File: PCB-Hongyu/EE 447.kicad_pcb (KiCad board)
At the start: 4 copper layers, 100 x 100 mm, 73 parts, among them J1 Conn_01x04_Pin, J2 503480-2600, J3 S2B-PH-SM4-TB, J5 Conn_01x02_Pin, J6 Conn_01x01_Pin, J7 Conn_01x01_Pin, J8 Conn_01x01_Pin, J9 Conn_01x02_Pin, Q1 BSS138, Q2 S8050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

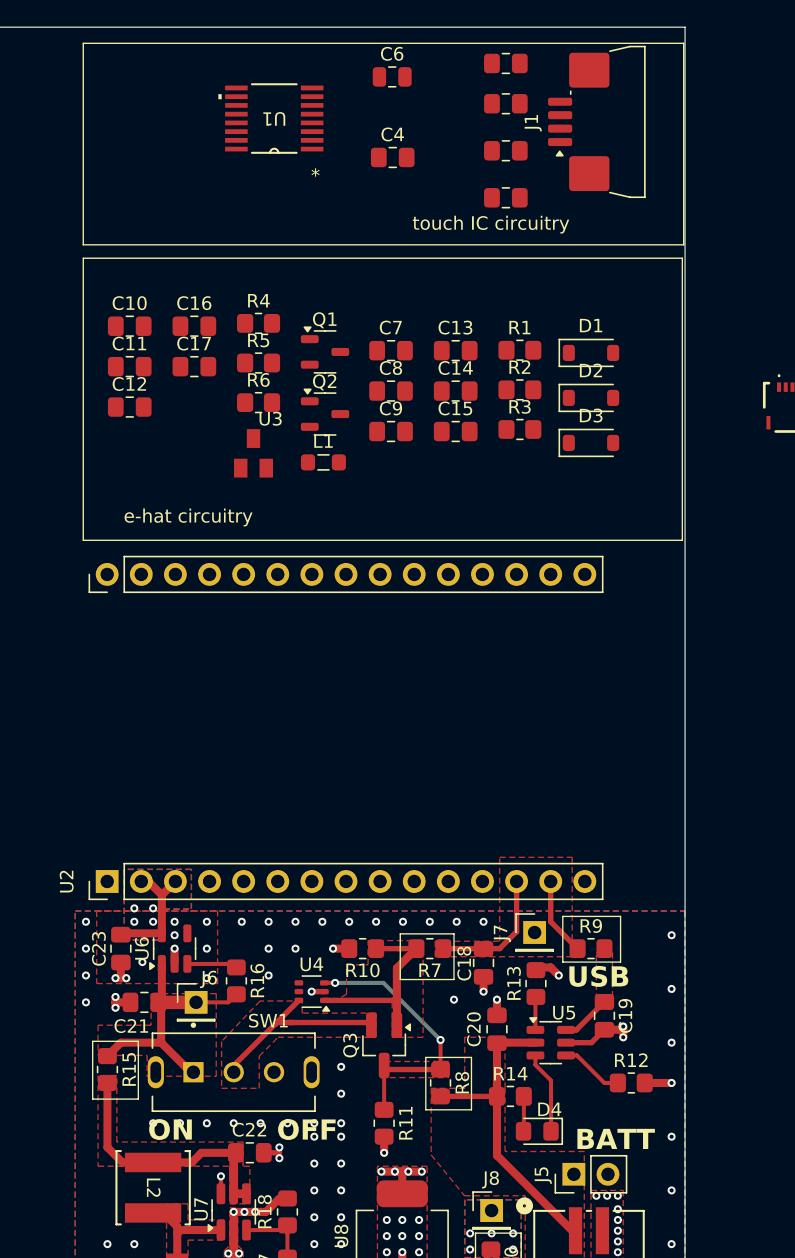
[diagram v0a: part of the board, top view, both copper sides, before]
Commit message: touch ic mostly routed
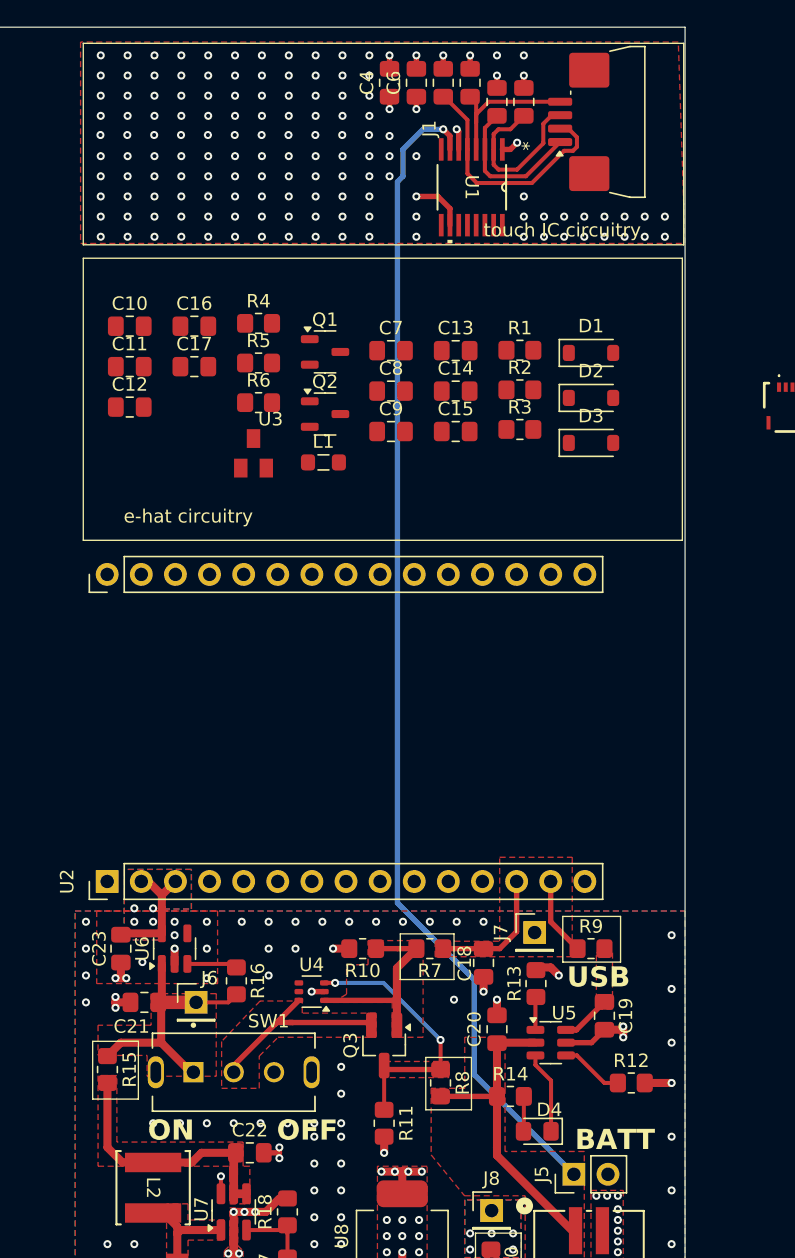
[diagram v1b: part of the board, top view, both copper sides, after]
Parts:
- C6: footprint Capacitor_SMD:C_0805_2012Metric -> Capacitor_SMD:C_0805_2012Metric_Pad1.18x1.45mm_HandSolder
- moved U1 15.6 mm to (215.1, 115.3), turned to -90 degrees
- moved C2 7.17 mm to (217.0, 109.0), turned to 90 degrees
- moved C5 6.88 mm to (213.0, 107.5), turned to 90 degrees
- moved C4 5.57 mm to (209.0, 107.5), turned to 90 degrees
- moved C3 3.03 mm to (215.0, 107.5), turned to 90 degrees
- moved C6 1.85 mm to (211.0, 107.5), turned to 90 degrees
- moved C1 1.34 mm to (219.0, 109.0), turned to 90 degrees
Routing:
- net +BATT: track 23.8 -> 111.0 mm, vias 0 -> 1
- net Net-(J1-Pin_2): track 0.00 -> 18.3 mm
- net Net-(J1-Pin_3): track 0.00 -> 12.8 mm
- net Net-(J1-Pin_4): track 0.00 -> 11.4 mm
- net Net-(J1-Pin_1): track 0.00 -> 11.3 mm
- net GND: track 48.3 -> 55.5 mm, vias 121 -> 263
- net +3.3V: track 9.32 -> 13.4 mm, vias 4 -> 5
- net +5V: track 0.00 -> 3.16 mm, vias 5 -> 8

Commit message: footprints
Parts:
- J2: value 503480-2600 -> FH34SRJ-24S-0.5SH_99_; footprint Custom:5034802600 -> Custom:FH34SRJ24S05SH99
- Q2: footprint Package_TO_SOT_SMD:SOT-23-3 -> Package_TO_SOT_THT:TO-92_Inline
- moved U3 68.8 mm to (267.6, 138.1)
- moved Q2 64.2 mm to (268.3, 129.0)
- moved Q1 59.8 mm to (263.1, 138.2)
- moved R4 59.8 mm to (258.1, 136.1)
- moved R5 59.8 mm to (258.1, 139.0)
- moved R6 59.8 mm to (258.1, 142.0)
- moved L1 59.2 mm to (263.0, 141.8)
- moved C11 59.0 mm to (248.5, 132.9)
- moved C17 59.0 mm to (253.3, 132.9)
- moved C10 59.0 mm to (248.5, 129.9)
- moved C12 59.0 mm to (248.5, 135.9)
- moved C16 59.0 mm to (253.3, 129.9)
- moved C13 40.0 mm to (253.3, 120.9)
- moved C14 40.0 mm to (253.3, 123.9)
- moved C15 40.0 mm to (253.3, 126.9)
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- renumbered J8 to J4, J9 to J8
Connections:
- net /Epaper/EPD_PWR renamed Net-(R3-Pad2)
- net CS_EPD renamed /Epaper/EPD_CS
- C10 pad 1: 3V3_EPD -> /Epaper/3V3_OUT
- C10 pad 2: GND -> /Epaper/BS
- C11 pad 2: GND -> /Epaper/BS
- C12 pad 2: GND -> /Epaper/BS
- C13 pad 2: GND -> /Epaper/BS
- C14 pad 2: GND -> /Epaper/BS
- C15 pad 2: GND -> /Epaper/BS
- C16 pad 2: GND -> /Epaper/BS
- C17 pad 1: +3.3V -> /Epaper/VCC_INT
- C17 pad 2: GND -> /Epaper/BS
- C7 pad 1: GND -> /Epaper/BS
- C7 pad 2: 3V3_EPD -> Net-(C7-Pad2)
- C9 pad 2: GND -> /Epaper/BS
- D1 pad 1: GND -> /Epaper/BS
- J2 pad 13: CLK -> /Epaper/EPD_SCK
- J2 pad 14: MOSI -> /Epaper/EPD_DIN
- J2 pad 15: 3V3_EPD -> /Epaper/3V3_OUT
- J2 pad 16: 3V3_EPD -> /Epaper/3V3_OUT
- J2 pad 17: GND -> /Epaper/BS
- J2 pad 8: GND -> /Epaper/BS
- J2 pad MP1: unconnected-(J2-MP1_1-PadMP1) -> /Epaper/BS
- J2 pad MP2: unconnected-(J2-MP1_2-PadMP2) -> /Epaper/BS
- L1 pad 1: 3V3_EPD -> Net-(C7-Pad2)
- Q1 pad 1: /Epaper/GDR -> Net-(Q1-G)
- Q1 pad 2: /Epaper/RESE -> Net-(Q1-S)
- Q2 pad 1: GND -> /Epaper/BS
- R1 pad 1: /Epaper/RESE -> Net-(Q1-S)
- R1 pad 2: GND -> /Epaper/BS
- R2 pad 1: GND -> /Epaper/BS
- R2 pad 2: /Epaper/GDR -> Net-(Q1-G)
- R3 pad 1: +3.3V -> /Epaper/VCC_INT
- R5 pad 1: +3.3V -> /Epaper/VCC_INT
- R6 pad 1: GND -> /Epaper/BS
- U3 pad 2: +3.3V -> /Epaper/VCC_INT
- U3 pad 3: 3V3_EPD -> unconnected-(U3-Pad3)

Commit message: adapter
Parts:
- added J9: 61302421121, Custom:61302421121, F.Cu at (144.5, 132.6)
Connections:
- net Net-(C11-Pad1) renamed /Epaper/SUB18
- net Net-(C12-Pad1) renamed /Epaper/SUB20
- net Net-(C14-Pad1) renamed /Epaper/SUB22
- net Net-(C16-Pad1) renamed /Epaper/SUB24
- net Net-(C9-Pad1) renamed /Epaper/SUB5

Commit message: i added stuff
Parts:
- moved J9 91.6 mm to (235.0, 118.4), turned to -90 degrees
- moved Q2 58.9 mm to (209.4, 127.3), turned to 90 degrees
- moved L1 57.1 mm to (206.0, 137.8), turned to -90 degrees
- moved U3 55.3 mm to (214.5, 123.0)
- moved D3 54.4 mm to (209.2, 130.5), turned to 180 degrees
- moved Q1 54.4 mm to (208.9, 133.8), turned to 180 degrees
- moved D1 54.2 mm to (210.5, 139.0), turned to -90 degrees
- moved D2 49.6 mm to (214.5, 138.8), turned to 90 degrees
- moved R1 45.5 mm to (213.0, 133.3)
- moved R2 45.4 mm to (213.0, 135.3), turned to 180 degrees
- moved R5 45.4 mm to (214.5, 126.5), turned to 180 degrees
- moved R6 45.0 mm to (214.5, 131.0), turned to 180 degrees
- moved C8 44.9 mm to (207.0, 140.8), turned to 180 degrees
- moved R4 44.3 mm to (214.5, 128.5)
- moved C7 44.0 mm to (208.0, 137.8), turned to 90 degrees
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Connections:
- C10 pad 2: /Epaper/BS -> GND
- C11 pad 2: /Epaper/BS -> GND
- C12 pad 2: /Epaper/BS -> GND
- C13 pad 2: /Epaper/BS -> GND
- C14 pad 2: /Epaper/BS -> GND
- C15 pad 2: /Epaper/BS -> GND
- C16 pad 2: /Epaper/BS -> GND
- C17 pad 1: /Epaper/VCC_INT -> +3.3V
- C17 pad 2: /Epaper/BS -> GND
- C7 pad 1: /Epaper/BS -> GND
- C9 pad 2: /Epaper/BS -> GND
- D1 pad 1: /Epaper/BS -> GND
- J2 pad 13: /Epaper/EPD_SCK -> CLK
- J2 pad 14: /Epaper/EPD_DIN -> MOSI
- J2 pad 17: /Epaper/BS -> GND
- J2 pad 8: /Epaper/BS -> GND
- J2 pad MP1: /Epaper/BS -> GND
- J2 pad MP2: /Epaper/BS -> GND
- J9 pad 13: /Epaper/EPD_DIN -> MOSI
- J9 pad 14: /Epaper/EPD_SCK -> CLK
- J9 pad 18: /Epaper/BS -> GND
- J9 pad 7: /Epaper/BS -> GND
- Q2 pad 1: /Epaper/BS -> GND
- R1 pad 2: /Epaper/BS -> GND
- R2 pad 1: /Epaper/BS -> GND
- R3 pad 1: /Epaper/VCC_INT -> +3.3V
- R5 pad 1: /Epaper/VCC_INT -> +3.3V
- R6 pad 1: /Epaper/BS -> GND
- U3 pad 2: /Epaper/VCC_INT -> +3.3V
- U3 pad 3: unconnected-(U3-Pad3) -> /Epaper/3V3_OUT
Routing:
- net /Epaper/VGL: track 0.00 -> 38.3 mm
- net /Epaper/VGH: track 0.00 -> 37.9 mm
- net /Epaper/SUB22: track 0.00 -> 25.5 mm
- net /Epaper/3V3_OUT: track 0.00 -> 21.6 mm, vias 0 -> 3
- net GND: track 55.5 -> 75.6 mm, vias 263 -> 279
- net /Epaper/SUB20: track 0.00 -> 19.6 mm
- net /Epaper/SUB18: track 0.00 -> 18.8 mm
- net /Epaper/SUB5: track 0.00 -> 16.8 mm
- net /Epaper/SUB24: track 0.00 -> 16.2 mm
- net Net-(D3-A): track 0.00 -> 15.1 mm
- net CLK: track 0.00 -> 13.0 mm
- net /Epaper/EPD_DC: track 0.00 -> 12.3 mm
- net /Epaper/RESE: track 0.00 -> 12.3 mm
- net /Epaper/EPD_BUSY: track 0.00 -> 11.7 mm
- net /Epaper/GDR: track 0.00 -> 10.6 mm
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- added copper zone on In2.Cu, net /Epaper/3V3_OUT
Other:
- board size 100 x 100 mm -> 109.5 x 100 mm

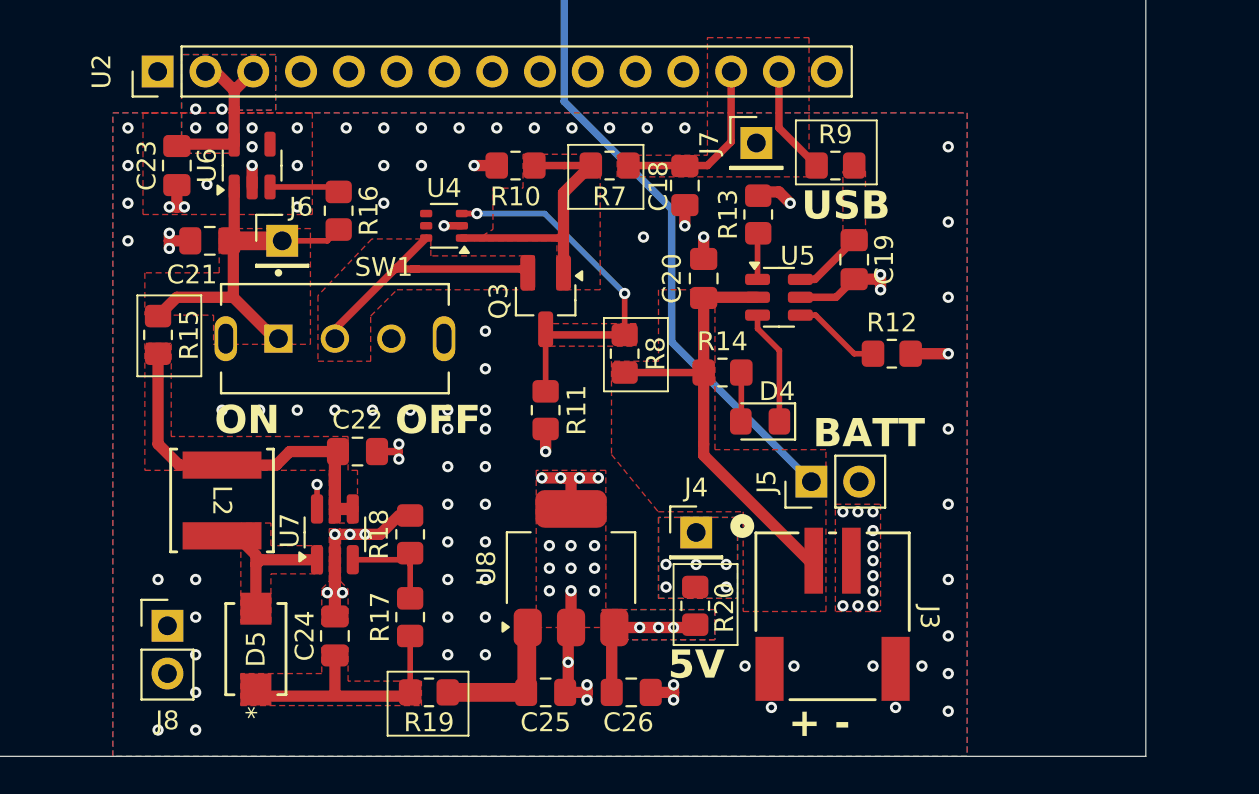
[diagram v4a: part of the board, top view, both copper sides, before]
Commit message: changed inductor. did some SPICE sims
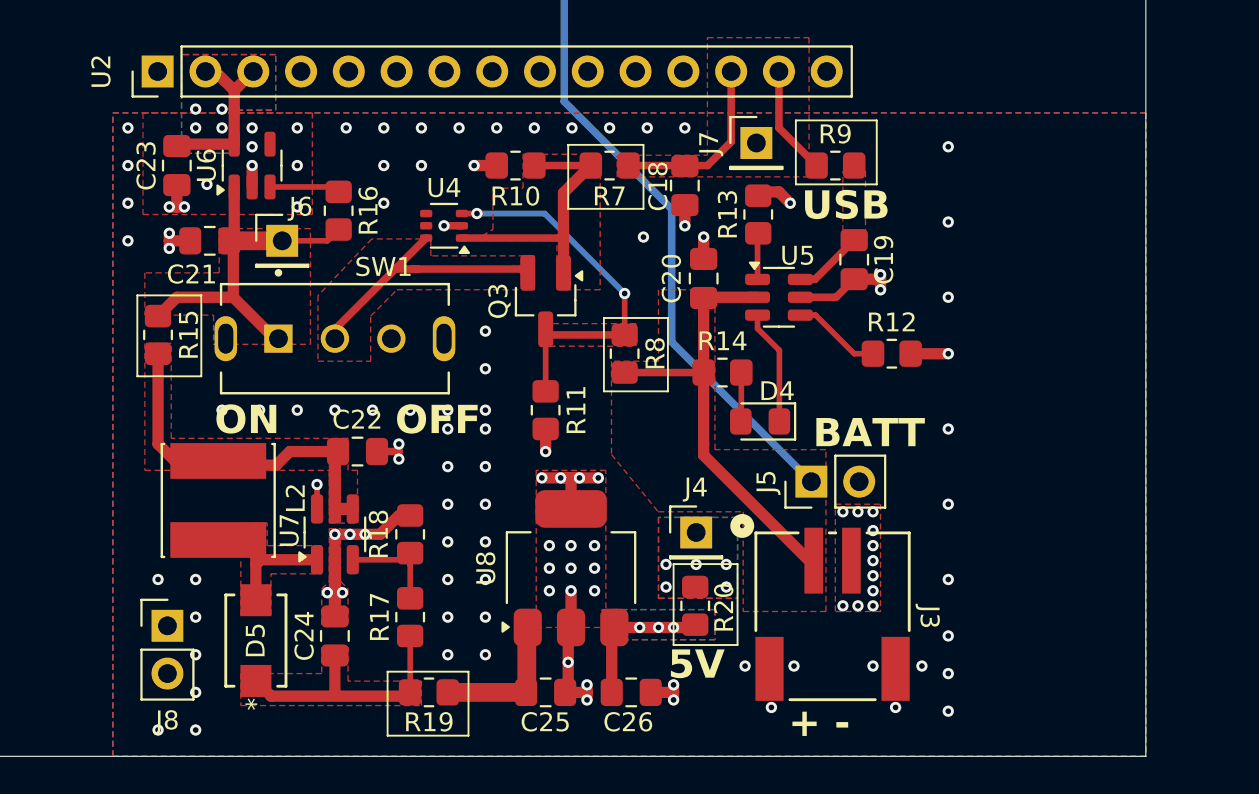
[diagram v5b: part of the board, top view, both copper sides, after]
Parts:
- L2: footprint Library:IND_SWPA5040S_SNL -> Library:IND_VLS6045AF-3R3N
- moved D5 0.45 mm to (193.2, 197.2)
- moved L2 0.20 mm to (191.2, 189.8)
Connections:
- U4 pad 5: unconnected-(U4-ST-Pad5) -> GND
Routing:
- net /Power/BOOST_VOUT: track 12.0 -> 13.2 mm

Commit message: yur
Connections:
- J2 pad 10: /Epaper/EPD_RST -> EPD_RST
- J2 pad 11: /Epaper/EPD_DC -> EPD_DC
- J2 pad 12: /Epaper/EPD_CS -> EPD_CS
- J2 pad 9: /Epaper/EPD_BUSY -> EPD_BUSY
- J9 pad 10: /Epaper/EPD_BUSY -> EPD_BUSY
- J9 pad 11: /Epaper/EPD_CS -> EPD_CS
- J9 pad 12: /Epaper/EPD_DC -> EPD_DC
- J9 pad 9: /Epaper/EPD_RST -> EPD_RST
- U2 pad 25: unconnected-(U2-IO5-Pad25) -> EPD_DC
- U2 pad 26: unconnected-(U2-IO4-Pad26) -> EPD_RST
- U2 pad 28: unconnected-(U2-IO18-Pad28) -> EPD_BUSY
- U2 pad 5: unconnected-(U2-IO3-Pad5) -> EPD_CS
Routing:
- net EPD_CS: track 0.00 -> 79.6 mm
- net MOSI: track 10.2 -> 65.0 mm
- net CLK: track 13.0 -> 64.2 mm
- net EPD_BUSY: track 0.00 -> 36.4 mm, vias 0 -> 1
- net EPD_DC: track 0.00 -> 35.5 mm, vias 0 -> 1
- net EPD_RST: track 0.00 -> 34.9 mm, vias 0 -> 1
- net /Epaper/EPD_DC: track 12.3 -> 0.00 mm
- net /Epaper/EPD_BUSY: track 11.7 -> 0.00 mm
- net /Epaper/EPD_CS: track 9.59 -> 0.00 mm
- net /Epaper/EPD_RST: track 8.95 -> 0.00 mm

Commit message: routed spi
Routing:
- net CS_TSC: track 0.00 -> 87.9 mm
- net MISO: track 0.00 -> 61.5 mm
- net MOSI: track 65.0 -> 100.0 mm
- net GND: track 75.6 -> 93.9 mm, vias 279 -> 287
- net CLK: track 64.2 -> 80.1 mm

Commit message: almost done
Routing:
- net +BATT: track 111.0 -> 124.7 mm
- net GND: vias 287 -> 218
- net +3.3V: vias 9 -> 103
